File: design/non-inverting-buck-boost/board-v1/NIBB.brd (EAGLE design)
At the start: 100 x 80 mm, 0 parts

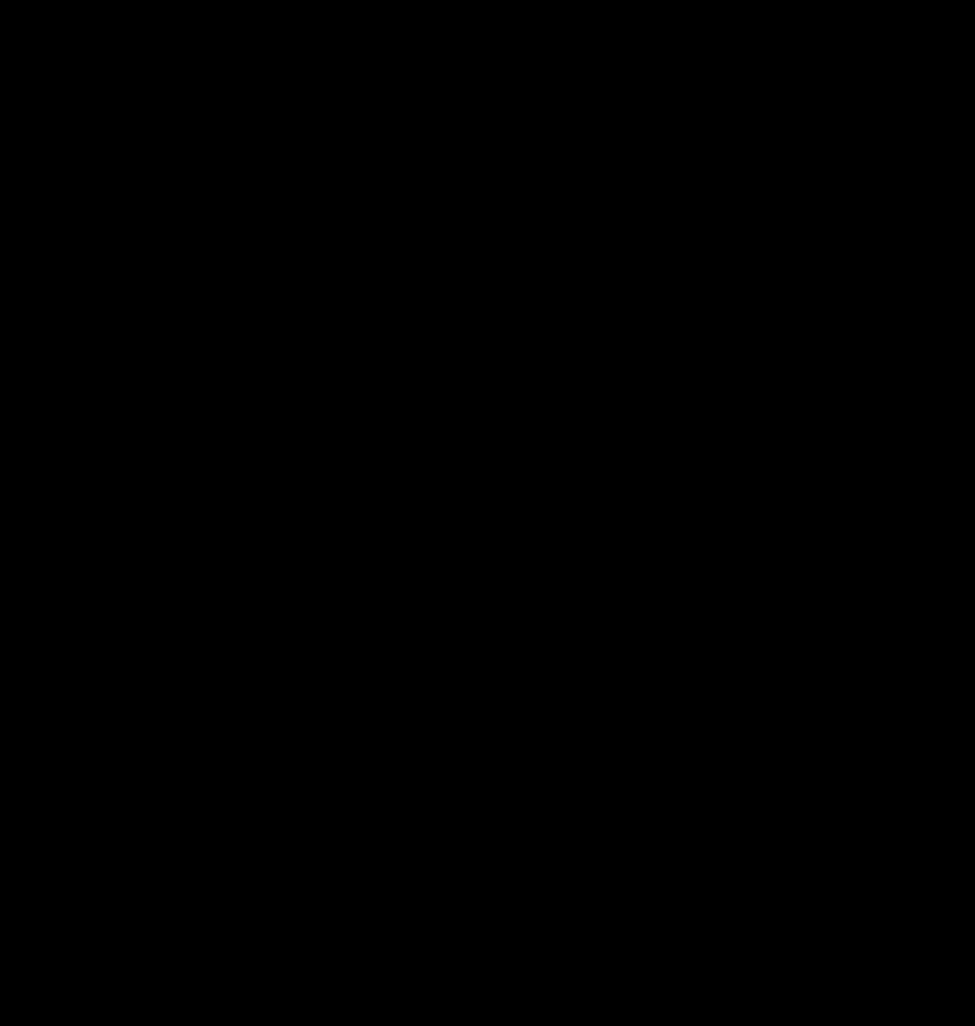
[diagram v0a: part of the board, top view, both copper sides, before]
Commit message: added switches
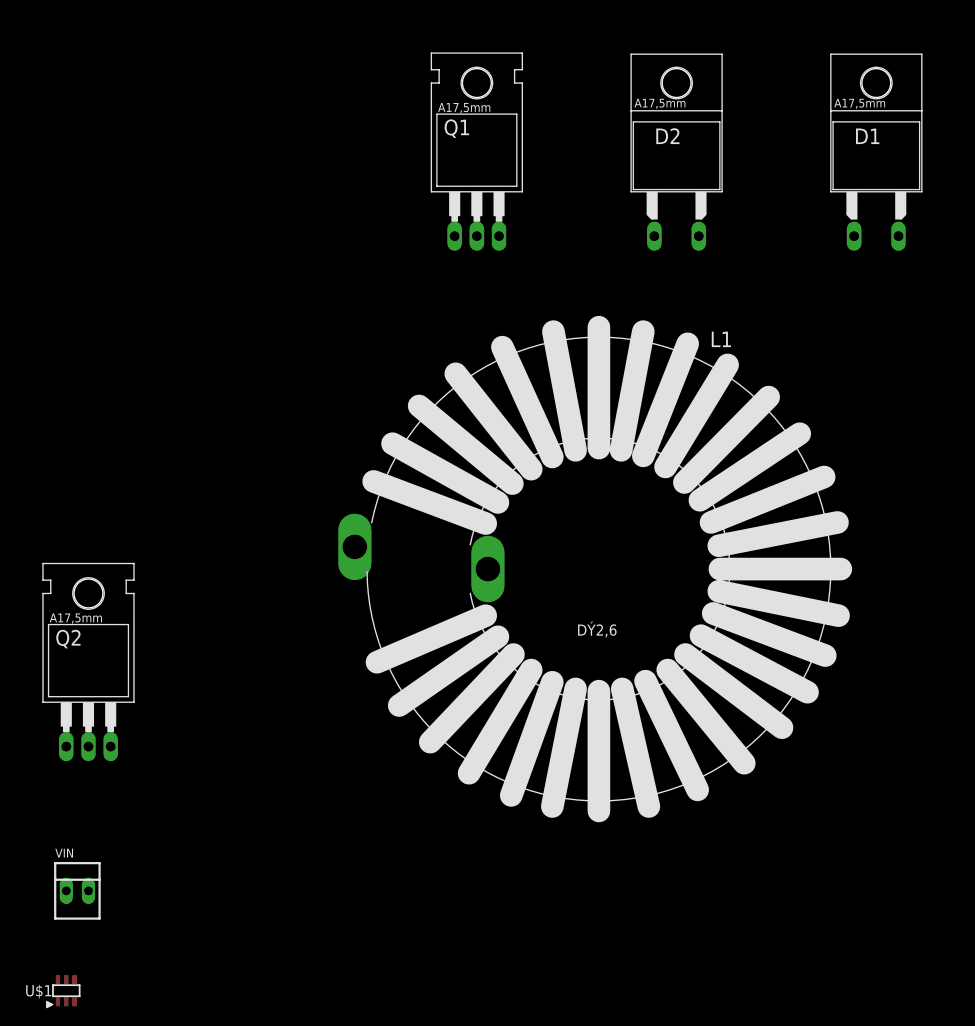
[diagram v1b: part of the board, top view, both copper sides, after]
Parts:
- added D1, D2: MUR820, diode:C221B1A
- added L1: RKE16, inductors:RKE16
- added Q1, Q2: IRLZ44Z, transistor-power:TO220BH
- added U$1: ZXGD3006E6, felippe:SOT23
- added VIN: 2PIN, con-molex:22-23-2021
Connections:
- new net N$1: D1.C, L1.1, Q1.S
- new net N$2: L1.2, Q2.D
- new net N$3: Q1.D, VIN.1
- new net N$4: D1.A, Q2.S, VIN.2

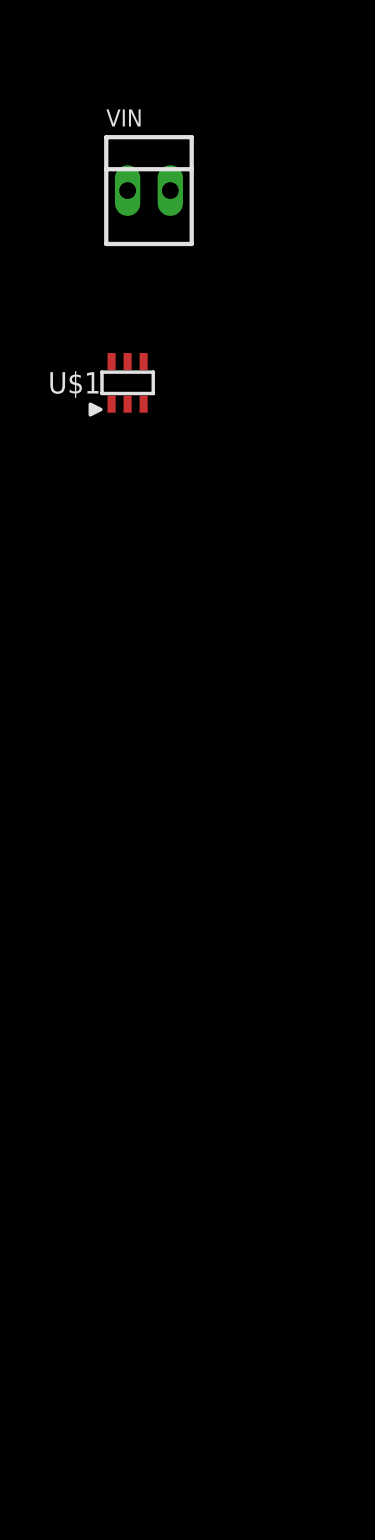
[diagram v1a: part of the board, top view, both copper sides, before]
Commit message: added connectors
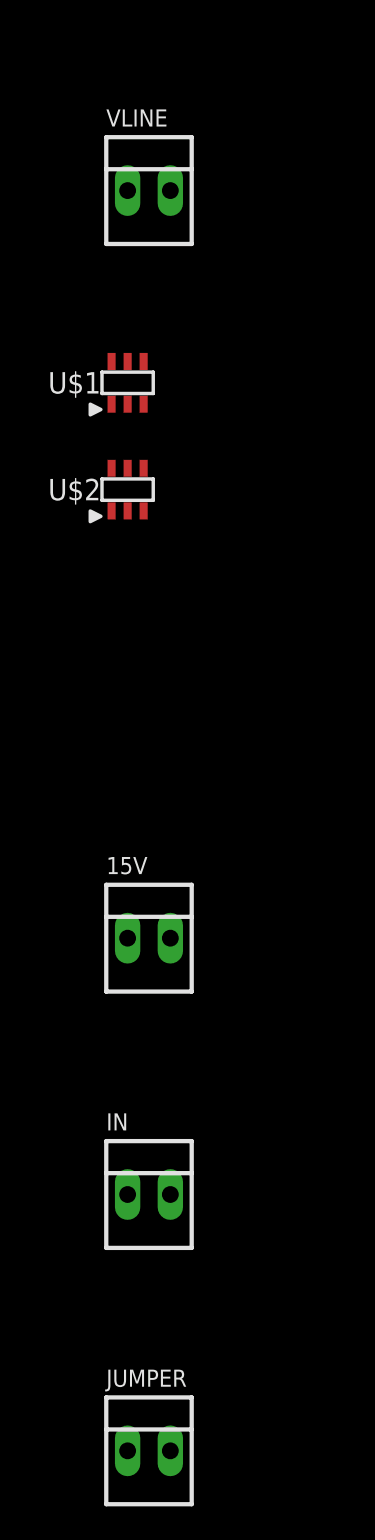
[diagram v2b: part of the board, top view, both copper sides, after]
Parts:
- added 15V, IN, JUMPER: (no value), con-molex:22-23-2021
- added U$2: ZXGD3006E6, felippe:SOT23
- VLINE: value 2PIN -> (none)
- renumbered VIN to VLINE
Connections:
- new net N$5: Q1.G, U$1.4, U$1.6
- new net N$6: Q2.G, U$2.4, U$2.6
- net N$2: now also D2.A
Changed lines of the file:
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@@
 <element name="L1" library="inductors" package="RKE16" value="RKE16" x="-43.18" y="-29.21"/>
 <element name="Q2" library="transistor-power" package="TO220BH" value="IRLZ44Z" x="-101.6" y="-43.18"/>
-<element name="VIN" library="con-molex" package="22-23-2021" value="2PIN" x="-102.87" y="-66.04">
+<element name="VLINE" library="con-molex" package="22-23-2021" value="" x="-102.87" y="-66.04">
 <attribute name="MF" value="MOLEX" x="-102.87" y="-66.04" size="1.778" layer="27" display="off"/>
 <attribute name="MPN" value="22-23-2021" x="-102.87" y="-66.04" size="1.778" layer="27" display="off"/>
@@
 </element>
 <element name="U$1" library="felippe" package="SOT23" value="ZXGD3006E6" x="-104.14" y="-77.47"/>
+<element name="U$2" library="felippe" package="SOT23" value="ZXGD3006E6" x="-104.14" y="-83.82"/>
+<element name="15V" library="con-molex" package="22-23-2021" value="" x="-102.87" y="-110.49">
+<attribute name="MF" value="MOLEX" x="-102.87" y="-110.49" size="1.778" layer="27" display="off"/>
+<attribute name="MPN" value="22-23-2021" x="-102.87" y="-110.49" size="1.778" layer="27" display="off"/>
+<attribute name="OC_FARNELL" value="1462926" x="-102.87" y="-110.49" size="1.778" layer="27" display="off"/>
+<attribute name="OC_NEWARK" value="25C3832" x="-102.87" y="-110.49" size="1.778" layer="27" display="off"/>
+</element>
+<element name="IN" library="con-molex" package="22-23-2021" value="" x="-102.87" y="-125.73">
+<attribute name="MF" value="MOLEX" x="-102.87" y="-125.73" size="1.778" layer="27" display="off"/>
+<attribute name="MPN" value="22-23-2021" x="-102.87" y="-125.73" size="1.778" layer="27" display="off"/>
+<attribute name="OC_FARNELL" value="1462926" x="-102.87" y="-125.73" size="1.778" layer="27" display="off"/>
+<attribute name="OC_NEWARK" value="25C3832" x="-102.87" y="-125.73" size="1.778" layer="27" display="off"/>
+</element>
+<element name="JUMPER" library="con-molex" package="22-23-2021" value="" x="-102.87" y="-140.97">
+<attribute name="MF" value="MOLEX" x="-102.87" y="-140.97" size="1.778" layer="27" display="off"/>
+<attribute name="MPN" value="22-23-2021" x="-102.87" y="-140.97" size="1.778" layer="27" display="off"/>
+<attribute name="OC_FARNELL" value="1462926" x="-102.87" y="-140.97" size="1.778" layer="27" display="off"/>
+<attribute name="OC_NEWARK" value="25C3832" x="-102.87" y="-140.97" size="1.778" layer="27" display="off"/>
+</element>
 </elements>
 <signals>
@@
 <contactref element="Q2" pad="D"/>
 <contactref element="L1" pad="2"/>
+<contactref element="D2" pad="A"/>
 <wire x1="-55.88" y1="-29.21" x2="-101.6" y2="-49.53" width="0" layer="19" extent="1-1"/>
+<wire x1="-31.75" y1="8.89" x2="-55.88" y2="-29.21" width="0" layer="19" extent="1-1"/>
 </signal>
 <signal name="N$4">
 <contactref element="Q2" pad="S"/>
 <contactref element="D1" pad="A"/>
-<contactref element="VIN" pad="2"/>
+<contactref element="VLINE" pad="2"/>
 <wire x1="-99.06" y1="-49.53" x2="-101.6" y2="-66.04" width="0" layer="19" extent="1-1"/>
 <wire x1="-8.89" y1="8.89" x2="-99.06" y2="-49.53" width="0" layer="19" extent="1-1"/>
@@
 <signal name="N$3">
 <contactref element="Q1" pad="D"/>
-<contactref element="VIN" pad="1"/>
+<contactref element="VLINE" pad="1"/>
 <wire x1="-57.15" y1="8.89" x2="-104.14" y2="-66.04" width="0" layer="19" extent="1-1"/>
 </signal>
+<signal name="N$5">
+<contactref element="U$1" pad="6"/>
+<contactref element="Q1" pad="G"/>
+<contactref element="U$1" pad="4"/>
+<wire x1="-103.1875" y1="-76.2" x2="-105.0925" y2="-76.2" width="0" layer="19" extent="1-1"/>
+<wire x1="-59.69" y1="8.89" x2="-103.1875" y2="-76.2" width="0" layer="19" extent="1-1"/>
+</signal>
+<signal name="N$6">
+<contactref element="U$2" pad="4"/>
+<contactref element="U$2" pad="6"/>
+<contactref element="Q2" pad="G"/>
+<wire x1="-103.1875" y1="-82.55" x2="-105.0925" y2="-82.55" width="0" layer="19" extent="1-1"/>
+<wire x1="-104.14" y1="-49.53" x2="-105.0925" y2="-82.55" width="0" layer="19" extent="1-1"/>
+</signal>
 </signals>

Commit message: updated connectors
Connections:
- new net 15V+: 15V.1, U$1.1, U$2.1
- new net 15V-: 15V.2, U$1.3, U$2.3
- new net IN1: IN.1, JUMPER.1, U$1.2
- new net IN2: IN.2, JUMPER.2, U$2.2
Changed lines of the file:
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@@
 <wire x1="-104.14" y1="-49.53" x2="-105.0925" y2="-82.55" width="0" layer="19" extent="1-1"/>
+</signal>
+<signal name="15V+">
+<contactref element="15V" pad="1"/>
+<contactref element="U$1" pad="1"/>
+<contactref element="U$2" pad="1"/>
+<wire x1="-105.0925" y1="-85.09" x2="-104.14" y2="-110.49" width="0" layer="19" extent="1-1"/>
+<wire x1="-105.0925" y1="-78.74" x2="-105.0925" y2="-85.09" width="0" layer="19" extent="1-1"/>
+</signal>
+<signal name="15V-">
+<contactref element="15V" pad="2"/>
+<contactref element="U$1" pad="3"/>
+<contactref element="U$2" pad="3"/>
+<wire x1="-103.1875" y1="-85.09" x2="-101.6" y2="-110.49" width="0" layer="19" extent="1-1"/>
+<wire x1="-103.1875" y1="-78.74" x2="-103.1875" y2="-85.09" width="0" layer="19" extent="1-1"/>
+</signal>
+<signal name="IN1">
+<contactref element="IN" pad="1"/>
+<contactref element="JUMPER" pad="1"/>
+<contactref element="U$1" pad="2"/>
+<wire x1="-104.14" y1="-125.73" x2="-104.14" y2="-140.97" width="0" layer="19" extent="1-1"/>
+<wire x1="-104.14" y1="-78.74" x2="-104.14" y2="-125.73" width="0" layer="19" extent="1-1"/>
+</signal>
+<signal name="IN2">
+<contactref element="IN" pad="2"/>
+<contactref element="JUMPER" pad="2"/>
+<contactref element="U$2" pad="2"/>
+<wire x1="-101.6" y1="-125.73" x2="-101.6" y2="-140.97" width="0" layer="19" extent="1-1"/>
+<wire x1="-104.14" y1="-85.09" x2="-101.6" y2="-125.73" width="0" layer="19" extent="1-1"/>
 </signal>
 </signals>

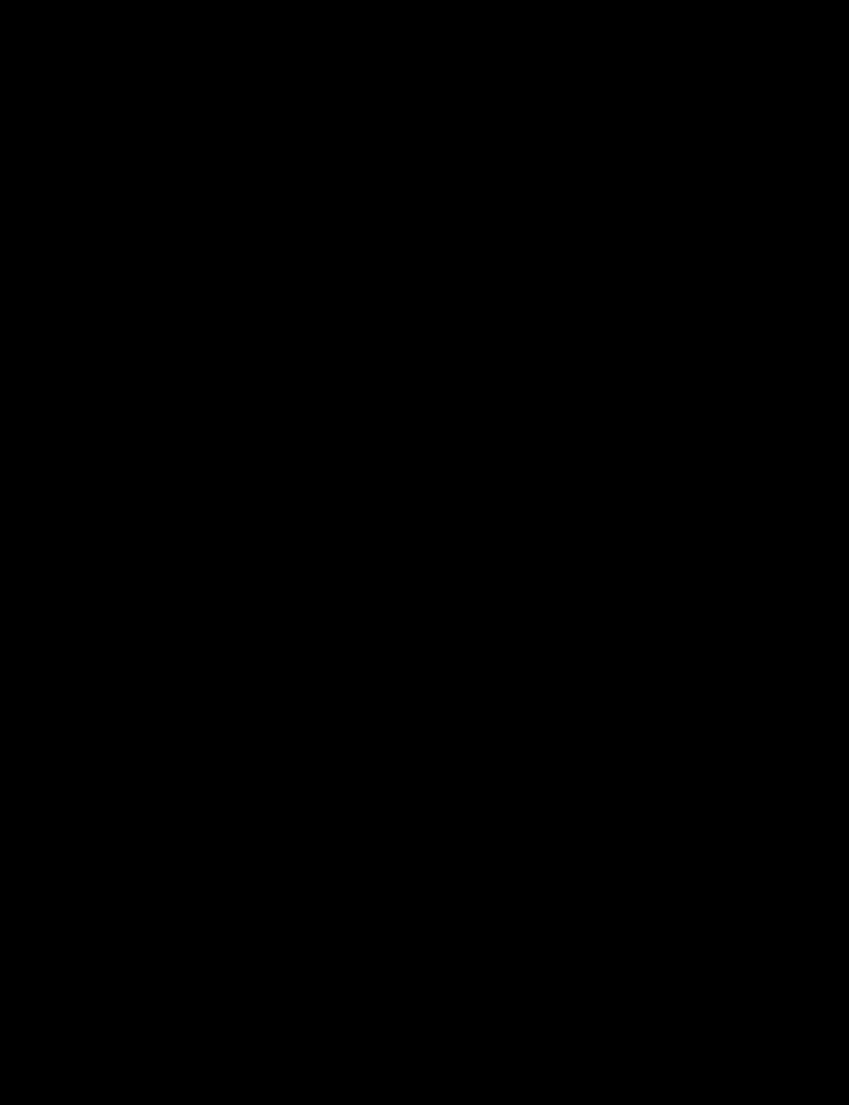
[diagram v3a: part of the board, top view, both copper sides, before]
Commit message: added output capacitor and connector
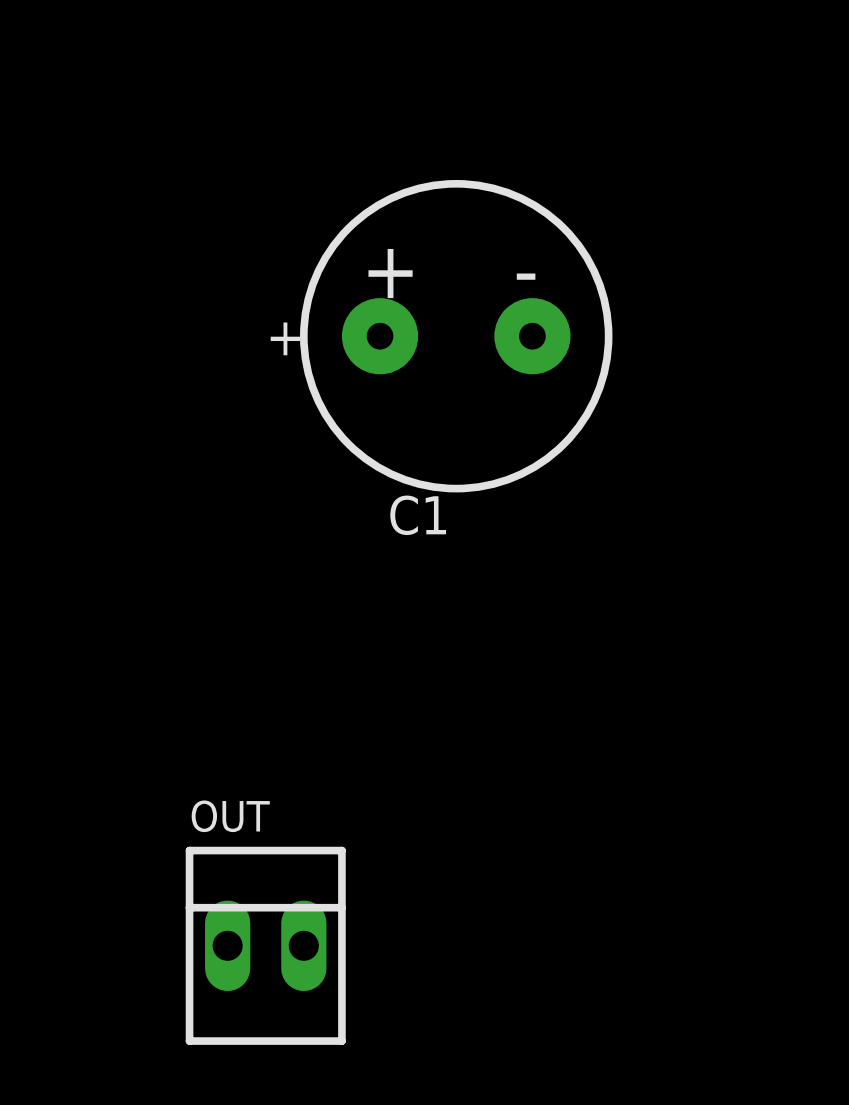
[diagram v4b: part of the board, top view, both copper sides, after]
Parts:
- added C1: (no value), capacitor:20ROUND40P
- added OUT: (no value), con-molex:22-23-2021
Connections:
- new net N$7: C1.+, D2.C, OUT.1
- net N$4: now also C1.-, OUT.2
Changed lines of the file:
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@@
 <attribute name="OC_NEWARK" value="25C3832" x="-102.87" y="-140.97" size="1.778" layer="27" display="off"/>
+</element>
+<element name="C1" library="capacitor" package="20ROUND40P" value="" x="-96.52" y="-161.29">
+<attribute name="DESC" value="Capacitor, polarized" x="-96.52" y="-161.29" size="1.778" layer="27" display="off"/>
+</element>
+<element name="OUT" library="con-molex" package="22-23-2021" value="" x="-102.87" y="-181.61">
+<attribute name="MF" value="MOLEX" x="-102.87" y="-181.61" size="1.778" layer="27" display="off"/>
+<attribute name="MPN" value="22-23-2021" x="-102.87" y="-181.61" size="1.778" layer="27" display="off"/>
+<attribute name="OC_FARNELL" value="1462926" x="-102.87" y="-181.61" size="1.778" layer="27" display="off"/>
+<attribute name="OC_NEWARK" value="25C3832" x="-102.87" y="-181.61" size="1.778" layer="27" display="off"/>
 </element>
 </elements>
 <signals>
-<signal name="N$1">
-<contactref element="Q1" pad="S"/>
-<contactref element="L1" pad="1"/>
-<contactref element="D1" pad="C"/>
-<wire x1="-54.61" y1="8.89" x2="-71.12" y2="-26.67" width="0" layer="19" extent="1-1"/>
-<wire x1="-13.97" y1="8.89" x2="-54.61" y2="8.89" width="0" layer="19" extent="1-1"/>
-</signal>
 <signal name="N$2">
-<contactref element="Q2" pad="D"/>
 <contactref element="L1" pad="2"/>
 <contactref element="D2" pad="A"/>
+<contactref element="Q2" pad="D"/>
 <wire x1="-55.88" y1="-29.21" x2="-101.6" y2="-49.53" width="0" layer="19" extent="1-1"/>
 <wire x1="-31.75" y1="8.89" x2="-55.88" y2="-29.21" width="0" layer="19" extent="1-1"/>
@@
 <signal name="N$4">
 <contactref element="Q2" pad="S"/>
+<contactref element="VLINE" pad="2"/>
+<contactref element="C1" pad="-"/>
 <contactref element="D1" pad="A"/>
-<contactref element="VLINE" pad="2"/>
+<contactref element="OUT" pad="2"/>
 <wire x1="-99.06" y1="-49.53" x2="-101.6" y2="-66.04" width="0" layer="19" extent="1-1"/>
+<wire x1="-93.98" y1="-161.29" x2="-101.6" y2="-66.04" width="0" layer="19" extent="1-1"/>
+<wire x1="-101.6" y1="-181.61" x2="-93.98" y2="-161.29" width="0" layer="19" extent="1-1"/>
 <wire x1="-8.89" y1="8.89" x2="-99.06" y2="-49.53" width="0" layer="19" extent="1-1"/>
 </signal>
@@
 <wire x1="-104.14" y1="-85.09" x2="-101.6" y2="-125.73" width="0" layer="19" extent="1-1"/>
 </signal>
+<signal name="N$7">
+<contactref element="D2" pad="C"/>
+<contactref element="C1" pad="+"/>
+<contactref element="OUT" pad="1"/>
+<wire x1="-99.06" y1="-161.29" x2="-104.14" y2="-181.61" width="0" layer="19" extent="1-1"/>
+<wire x1="-36.83" y1="8.89" x2="-99.06" y2="-161.29" width="0" layer="19" extent="1-1"/>
+</signal>
+<signal name="N$1">
+<contactref element="Q1" pad="S"/>
+<contactref element="L1" pad="1"/>
+<contactref element="D1" pad="C"/>
+<wire x1="-54.61" y1="8.89" x2="-71.12" y2="-26.67" width="0" layer="19" extent="1-1"/>
+<wire x1="-13.97" y1="8.89" x2="-54.61" y2="8.89" width="0" layer="19" extent="1-1"/>
+</signal>
 </signals>

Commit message: added components to layout
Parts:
- removed U$1, U$2: ZXGD3006E6, felippe:SOT23
- added IC1, IC2: (no value), felippe:SOT23
- Q1, Q2: value IRLZ44Z -> (none); device transistor-power:TO220BH -> felippe:TO220BV
- moved OUT 290.2 mm to (96.5, 29.2), turned to 270 degrees
- moved C1 263.2 mm to (86.4, 27.9), turned to 270 degrees
- moved JUMPER 196.8 mm to (21.6, 11.4), turned to 270 degrees
- moved Q2 193.1 mm to (72.4, 40.6), turned to 90 degrees
- moved IN 177.7 mm to (10.2, 11.4), turned to 270 degrees
- moved 15V 172.9 mm to (10.2, 20.3), turned to 270 degrees
- moved VLINE 147.0 mm to (10.2, 27.9), turned to 270 degrees
- moved D2 119.6 mm to (83.8, 34.3), turned to 180 degrees
- moved L1 97.7 mm to (44.5, 14.0), turned to 270 degrees
- moved Q1 89.9 mm to (25.4, 50.8)
- moved D1 80.8 mm to (58.4, 55.9)
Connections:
- net 15V+: now also IC1.1, IC2.1; no longer U$1.1, U$2.1
- net 15V-: now also IC1.3, IC2.3; no longer U$1.3, U$2.3
- net IN1: now also IC1.2; no longer U$1.2
- net IN2: now also IC2.2; no longer U$2.2
- net N$5: now also IC1.4, IC1.6; no longer U$1.4, U$1.6
- net N$6: now also IC2.4, IC2.6; no longer U$2.4, U$2.6
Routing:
- net N$4: track 0.00 -> 125.9 mm
- net N$5: track 0.00 -> 62.8 mm
- net IN2: track 0.00 -> 43.3 mm
- net 15V+: track 0.00 -> 42.9 mm
- net N$2: track 0.00 -> 42.6 mm
- net N$6: track 0.00 -> 38.6 mm
- net N$1: track 0.00 -> 34.8 mm
- net N$3: track 0.00 -> 29.1 mm
- net IN1: track 0.00 -> 27.7 mm
- net 15V-: track 0.00 -> 21.2 mm
- net N$7: track 0.00 -> 20.3 mm
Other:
- board size 100 x 80 mm -> 100 x 54.6 mm

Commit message: finished v1 layout
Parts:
- moved D2 27.1 mm to (78.7, 7.62)
- moved D1 14.9 mm to (53.3, 41.9)
- moved L1 14.9 mm to (39.4, 0.00)
- moved OUT 14.9 mm to (91.4, 15.2), turned to 90 degrees
- moved Q1 14.9 mm to (20.3, 36.8)
- moved Q2 14.9 mm to (67.3, 26.7)
- moved IC2 12.8 mm to (45.7, 8.89)
- moved JUMPER 8.52 mm to (14.0, 7.62)
- moved IC1 7.41 mm to (25.4, 17.8)
- moved C1 7.18 mm to (81.3, 22.9), turned to 90 degrees
- moved VLINE 6.35 mm to (5.08, 24.1)
- moved IN 6.35 mm to (5.08, 7.62)
- moved 15V 6.35 mm to (5.08, 16.5)
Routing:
- net 15V+: track 42.9 -> 93.8 mm
- net 15V-: track 21.2 -> 48.9 mm
- net N$2: track 42.6 -> 53.8 mm
- net N$7: track 20.3 -> 27.3 mm
- net N$5: track 62.8 -> 55.8 mm
- net N$3: track 29.1 -> 24.1 mm
- net N$6: track 38.6 -> 34.3 mm
- net N$4: track 125.9 -> 121.9 mm
- net IN2: track 43.3 -> 41.9 mm
- net IN1: track 27.7 -> 26.5 mm
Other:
- board size 100 x 54.6 mm -> 93.9 x 39.4 mm
